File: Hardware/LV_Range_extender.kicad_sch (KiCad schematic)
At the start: 17 parts, among them J1 Conn_01x03_Female, J2 Conn_01x03_Female, J3 Conn_01x04_Female, U1 ME6211A33M3G-N, U2 SN74LVC1T45DBV, U3 SN75176AD, U4 TS5A23159DGS

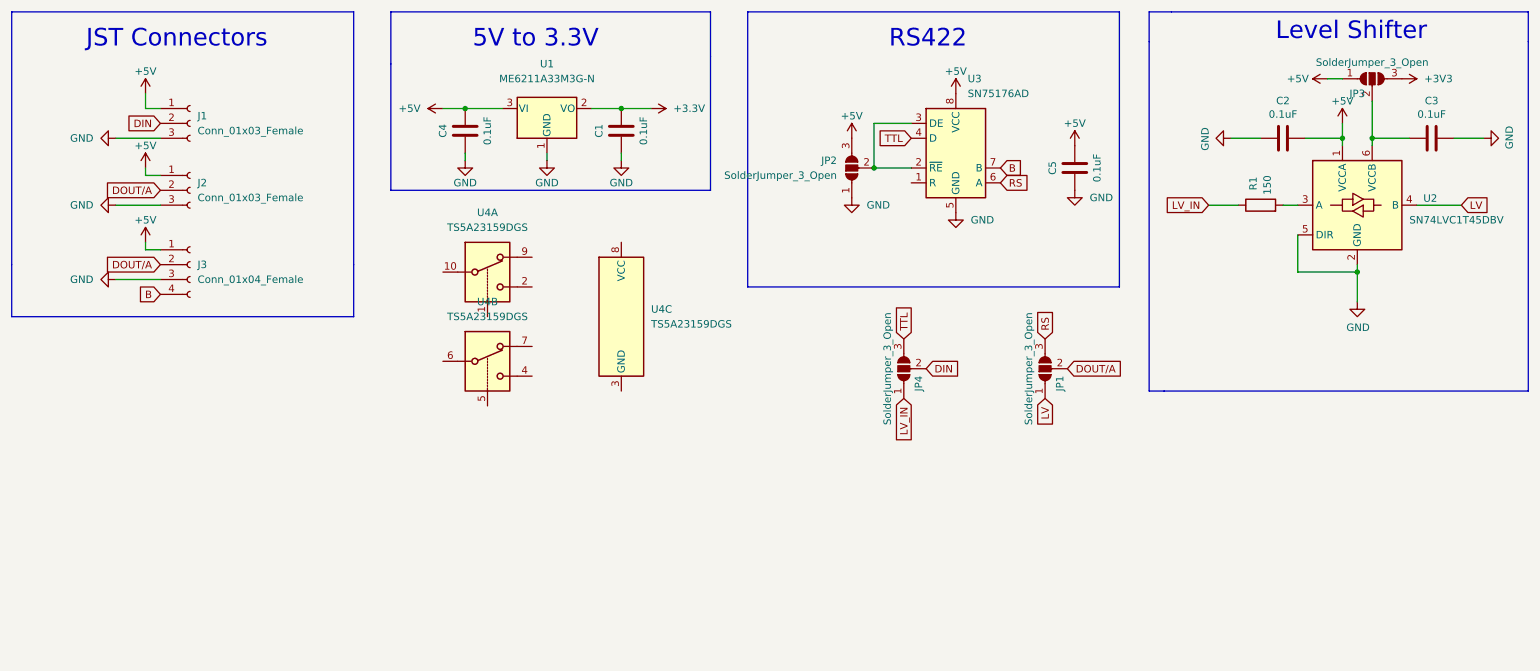
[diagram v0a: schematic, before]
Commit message: add multiplexer
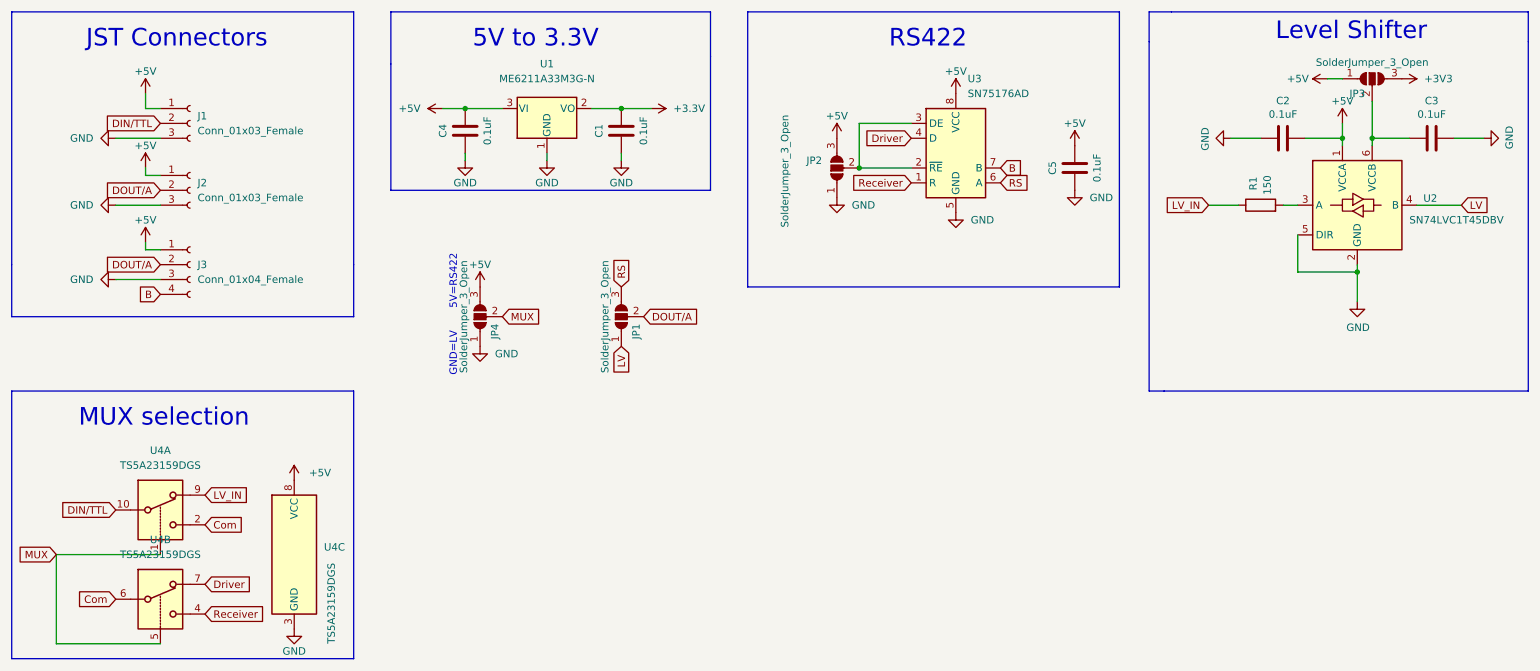
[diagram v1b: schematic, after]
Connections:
- net +5V: now also JP4.3 (B), U4.8 (VCC)
- net GND: now also JP4.1 (A), U4.3 (GND)
- net LV_IN: now also U4.9; no longer JP4.1 (A)
- net MUX: now reaches U4.1
- net MUX: now also JP4.2 (C), U4.5
- net DIN/TTL: now reaches U4.10
- net DIN/TTL: now also J1.2 (Pin_2)
- net Com: now reaches U4.2
- net Com: now also U4.6
- net Receiver: now reaches U4.4
- net Receiver: now also U3.1 (R)
- net Driver: now reaches U4.7
- net Driver: now also U3.4 (D)
- removed net DIN: J1.2 (Pin_2), JP4.2 (C)
- removed net TTL: JP4.3 (B), U3.4 (D)
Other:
- note added: "5V=RS422"
- note added: "GND=LV"
- note added: "MUX selection"
- moved on the sheet: JP1, JP2, JP4, U4A, U4B, U4C

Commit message: update multiplexing
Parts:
- removed JP2: SolderJumper_3_Open, Jumper:SolderJumper-3_P1.3mm_Open_Pad1.0x1.5mm, symbol Jumper:SolderJumper_3_Open
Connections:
- net +5V: now also C3.2, U2.6 (VCCB), U4.9; no longer C2.1, U2.1 (VCCA)
- net DOUT/A: now also JP1.1 (A); no longer JP1.2 (C)
- net GND: now also U4.2
- net RS: now also U4.6
- net RS_Enable: now reaches U3.2 (~{RE}), U3.3 (DE)
- net RS_Enable: now also U4.10
- removed net Com: U4.2, U4.6
- net DIN/TTL renamed LV_A
- net LV_A: now also R1.1; no longer U4.10
- net LV renamed LV_B
- net LV_B: now also JP1.2 (C); no longer JP1.1 (A)
- removed net LV_IN: R1.1, U4.9
- net MUX: no longer names the net of JP4.2 (C), U4.1, U4.5
- new net: C2.1, JP3.2 (C), U2.1 (VCCA)
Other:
- moved on the sheet: JP1, JP3, JP4, U4A, U4B, U4C

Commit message: Add ordered version V1
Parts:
- added JP2: SolderJumper_2_Open, Jumper:SolderJumper-2_P1.3mm_Open_Pad1.0x1.5mm, symbol Jumper:SolderJumper_2_Open
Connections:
- net +5V: now also C2.1, U2.1 (VCCA); no longer C3.2, U2.6 (VCCB)
- net DOUT/A: now also JP2.1 (A)
- net GND: no longer U2.5 (DIR)
- net LV_A: now also JP1.2 (C); no longer J1.2 (Pin_2)
- net LV_B: now also J1.2 (Pin_2); no longer JP1.2 (C)
- net RS: no longer U3.6 (A)
- net MUX: now reaches JP4.2 (C), U4.1, U4.5
- net MUX: now also U2.5 (DIR)
- new net: C3.2, JP3.2 (C), U2.6 (VCCB)
- new net: JP2.2 (B), U3.6 (A)
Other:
- moved on the sheet: JP3
